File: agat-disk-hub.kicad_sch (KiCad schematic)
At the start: 14 parts, among them J1 IDC‐20, J2 IDC‐20, J3 IDC‐34, J4 IDC‐10, J5 KK‐4

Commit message: refactor: rename project to agat-disk-hub; add URL to back side; add J5 label
Old project name was agat_disk_adapter.
The permanent URL of the project is now http://museum.computer/re/agat-disk-hub
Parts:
- J1, J2: footprint agat_disk_adapter:IDC-20_header_vertical_rotation180 -> agat-disk-hub:IDC-20_header_vertical_rotation180
- J3: footprint agat_disk_adapter:IDC-34_header_vertical_rotation0 -> agat-disk-hub:IDC-34_header_vertical_rotation0
- J4: footprint agat_disk_adapter:IDC-10_header_vertical_rotation270 -> agat-disk-hub:IDC-10_header_vertical_rotation270
- J5: footprint agat_disk_adapter:Molex_KK-4_vertical_rotation0 -> agat-disk-hub:Molex_KK-4_vertical_rotation0
- JP1, JP2: footprint agat_disk_adapter:jumper_pins_solder_drop_vertical -> agat-disk-hub:jumper_pins_solder_drop_vertical
- R2: footprint agat_disk_adapter:jumper_1206_solder_drop -> agat-disk-hub:jumper_1206_solder_drop
- XP1: footprint agat_disk_adapter:Eltra-26M -> agat-disk-hub:Eltra-26M; symbol agat_disk_adapter:Eltra-26M -> agat-disk-hub:Eltra-26M
- XS1: footprint agat_disk_adapter:Eltra-26F -> agat-disk-hub:Eltra-26F; symbol agat_disk_adapter:Eltra-26F -> agat-disk-hub:Eltra-26F
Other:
- company: КИБЕР-МУЗЕЙ, МУРОМ - Михаил Шевченко - mike.shevchenko@gmail.com -> КИБЕР‐МУЗЕЙ, МУРОМ, Михаил Шевченко, http://museum.computer/re/agat-disk-hub
- title: AGAT DISK ADAPTER -> AGAT-DISK-HUB
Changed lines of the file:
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@@
 	(paper "A5" portrait)
 	(title_block
-		(title "AGAT DISK ADAPTER")
+		(title "AGAT-DISK-HUB")
 		(date "2026-09")
 		(rev "V1")
-		(company "КИБЕР-МУЗЕЙ, МУРОМ - Михаил Шевченко - mike.shevchenko@gmail.com")
-		(comment 1 "- Подключение КНГМД - штатным кабелем, либо шлейфом с СНП34-30 на IDC-20,")
-		(comment 2 "- Сигнал \"Выбор Блока\" для 2-го дисковода (ВБ2) можно завести через -12|DE2.")
-		(comment 3 "- Назначение дисководов 1-м и 2-м можно выполнить джамперами либо тумблерами.")
+		(company "КИБЕР‐МУЗЕЙ, МУРОМ, Михаил Шевченко, http://museum.computer/re/agat-disk-hub")
+		(comment 1 "- Подключение КНГМД - штатным кабелем, либо шлейфом с СНП34‐30 на IDC‐20.")
+		(comment 2 "- Сигнал \"Выбор Блока\" для 2‐го дисковода (ВБ2) можно завести через -12|DE2.")
+		(comment 3 "- Назначение дисководов 1‐м/2‐м можно выполнить джамперами либо тумблерами.")
 		(comment 4 "Плата для подключения дисководов 140К и их эмуляторов к КНГМД Агат-7 и Apple 2.")
 	)
@@
 	)
 	(symbol
-		(lib_id "agat_disk_adapter:Eltra-26M")
+		(lib_id "agat-disk-hub:Eltra-26M")
 		(at 91.44 74.93 0)
 		(unit 1)
@@
 			)
 		)
-		(property "Footprint" "agat_disk_adapter:Eltra-26M"
+		(property "Footprint" "agat-disk-hub:Eltra-26M"
 			(at 91.44 74.93 0)
 			(hide yes)
@@
 		)
 		(instances
-			(project "agat_disk_adapter"
+			(project "agat-disk-hub"
 				(path "/e6908ff4-84b7-4cdb-b4c1-fd2e829eca09"
 					(reference "XP1")
@@
 		)
 		(instances
-			(project "agat_disk_adapter"
+			(project "agat-disk-hub"
 				(path "/e6908ff4-84b7-4cdb-b4c1-fd2e829eca09"
 					(reference "#PWR06")
@@
 		)
 		(instances
-			(project "agat_disk_adapter"
+			(project "agat-disk-hub"
 				(path "/e6908ff4-84b7-4cdb-b4c1-fd2e829eca09"
 					(reference "XS404")
@@
 		)
 		(instances
-			(project "agat_disk_adapter"
+			(project "agat-disk-hub"
 				(path "/e6908ff4-84b7-4cdb-b4c1-fd2e829eca09"
 					(reference "#PWR09")
@@
 		)
 		(instances
-			(project "agat_disk_adapter"
+			(project "agat-disk-hub"
 				(path "/e6908ff4-84b7-4cdb-b4c1-fd2e829eca09"
 					(reference "#PWR011")
@@
 	)
 	(symbol
-		(lib_id "agat_disk_adapter:Eltra-26F")
+		(lib_id "agat-disk-hub:Eltra-26F")
 		(at 91.44 39.37 0)
 		(unit 1)
@@
 			)
 		)
-		(property "Footprint" "agat_disk_adapter:Eltra-26F"
+		(property "Footprint" "agat-disk-hub:Eltra-26F"
 			(at 91.44 39.37 0)
 			(hide yes)
@@
 		)
 		(instances
-			(project "agat_disk_adapter"
+			(project "agat-disk-hub"
 				(path "/e6908ff4-84b7-4cdb-b4c1-fd2e829eca09"
 					(reference "XS1")
@@
 			)
 		)
-		(property "Footprint" "agat_disk_adapter:IDC-34_header_vertical_rotation0"
+		(property "Footprint" "agat-disk-hub:IDC-34_header_vertical_rotation0"
 			(at 106.68 152.4 0)
 			(hide yes)
@@
 		)
 		(instances
-			(project "agat_disk_adapter"
+			(project "agat-disk-hub"
 				(path "/e6908ff4-84b7-4cdb-b4c1-fd2e829eca09"
 					(reference "J3")
@@
 		)
 		(instances
-			(project "agat_disk_adapter"
+			(project "agat-disk-hub"
 				(path "/e6908ff4-84b7-4cdb-b4c1-fd2e829eca09"
 					(reference "#PWR02")
@@
 			)
 		)
-		(property "Footprint" "agat_disk_adapter:Molex_KK-4_vertical_rotation0"
+		(property "Footprint" "agat-disk-hub:Molex_KK-4_vertical_rotation0"
 			(at 40.64 128.27 0)
 			(hide yes)
@@
 		)
 		(instances
-			(project "agat_disk_adapter"
+			(project "agat-disk-hub"
 				(path "/e6908ff4-84b7-4cdb-b4c1-fd2e829eca09"
 					(reference "J5")
@@
 			)
 		)
-		(property "Footprint" "agat_disk_adapter:IDC-20_header_vertical_rotation180"
+		(property "Footprint" "agat-disk-hub:IDC-20_header_vertical_rotation180"
 			(at 111.76 121.92 0)
 			(hide yes)
@@
 		)
 		(instances
-			(project "agat_disk_adapter"
+			(project "agat-disk-hub"
 				(path "/e6908ff4-84b7-4cdb-b4c1-fd2e829eca09"
 					(reference "J2")
@@
 		)
 		(instances
-			(project "agat_disk_adapter"
+			(project "agat-disk-hub"
 				(path "/e6908ff4-84b7-4cdb-b4c1-fd2e829eca09"
 					(reference "#PWR04")
@@
 		)
 		(instances
-			(project "agat_disk_adapter"
+			(project "agat-disk-hub"
 				(path "/e6908ff4-84b7-4cdb-b4c1-fd2e829eca09"
 					(reference "#PWR08")
@@
 		)
 		(instances
-			(project "agat_disk_adapter"
+			(project "agat-disk-hub"
 				(path "/e6908ff4-84b7-4cdb-b4c1-fd2e829eca09"
 					(reference "R1")
@@
 			)
 		)
-		(property "Footprint" "agat_disk_adapter:jumper_pins_solder_drop_vertical"
+		(property "Footprint" "agat-disk-hub:jumper_pins_solder_drop_vertical"
 			(at 129.54 132.08 0)
 			(hide yes)
@@
 		)
 		(instances
-			(project "agat_disk_adapter"
+			(project "agat-disk-hub"
 				(path "/e6908ff4-84b7-4cdb-b4c1-fd2e829eca09"
 					(reference "JP2")
@@
 			)
 		)
-		(property "Footprint" "agat_disk_adapter:jumper_1206_solder_drop"
+		(property "Footprint" "agat-disk-hub:jumper_1206_solder_drop"
 			(at 41.91 113.792 90)
 			(hide yes)
@@
 		)
 		(instances
-			(project "agat_disk_adapter"
+			(project "agat-disk-hub"
 				(path "/e6908ff4-84b7-4cdb-b4c1-fd2e829eca09"
 					(reference "R2")
@@
 			)
 		)
-		(property "Footprint" "agat_disk_adapter:IDC-10_header_vertical_rotation270"
+		(property "Footprint" "agat-disk-hub:IDC-10_header_vertical_rotation270"
 			(at 40.64 101.6 0)
 			(hide yes)
@@
 		)
 		(instances
-			(project "agat_disk_adapter"
+			(project "agat-disk-hub"
 				(path "/e6908ff4-84b7-4cdb-b4c1-fd2e829eca09"
 					(reference "J4")
@@
 		)
 		(instances
-			(project "agat_disk_adapter"
+			(project "agat-disk-hub"
 				(path "/e6908ff4-84b7-4cdb-b4c1-fd2e829eca09"
 					(reference "XT1")
@@
 		)
 		(instances
-			(project "agat_disk_adapter"
+			(project "agat-disk-hub"
 				(path "/e6908ff4-84b7-4cdb-b4c1-fd2e829eca09"
 					(reference "JP3")
@@
 		)
 		(instances
-			(project "agat_disk_adapter"
+			(project "agat-disk-hub"
 				(path "/e6908ff4-84b7-4cdb-b4c1-fd2e829eca09"
 					(reference "#PWR010")
@@
 		)
 		(instances
-			(project "agat_disk_adapter"
+			(project "agat-disk-hub"
 				(path "/e6908ff4-84b7-4cdb-b4c1-fd2e829eca09"
 					(reference "XS404")
@@
 		)
 		(instances
-			(project "agat_disk_adapter"
+			(project "agat-disk-hub"
 				(path "/e6908ff4-84b7-4cdb-b4c1-fd2e829eca09"
 					(reference "#PWR012")
@@
 		)
 		(instances
-			(project "agat_disk_adapter"
+			(project "agat-disk-hub"
 				(path "/e6908ff4-84b7-4cdb-b4c1-fd2e829eca09"
 					(reference "XS404")
@@
 		)
 		(instances
-			(project "agat_disk_adapter"
+			(project "agat-disk-hub"
 				(path "/e6908ff4-84b7-4cdb-b4c1-fd2e829eca09"
 					(reference "#PWR01")
@@
 		)
 		(instances
-			(project "agat_disk_adapter"
+			(project "agat-disk-hub"
 				(path "/e6908ff4-84b7-4cdb-b4c1-fd2e829eca09"
 					(reference "#PWR07")
@@
 		)
 		(instances
-			(project "agat_disk_adapter"
+			(project "agat-disk-hub"
 				(path "/e6908ff4-84b7-4cdb-b4c1-fd2e829eca09"
 					(reference "#PWR05")
@@
 			)
 		)
-		(property "Footprint" "agat_disk_adapter:IDC-20_header_vertical_rotation180"
+		(property "Footprint" "agat-disk-hub:IDC-20_header_vertical_rotation180"
 			(at 111.76 93.98 0)
 			(hide yes)
@@
 		)
 		(instances
-			(project "agat_disk_adapter"
+			(project "agat-disk-hub"
 				(path "/e6908ff4-84b7-4cdb-b4c1-fd2e829eca09"
 					(reference "J1")
@@
 		)
 		(instances
-			(project "agat_disk_adapter"
+			(project "agat-disk-hub"
 				(path "/e6908ff4-84b7-4cdb-b4c1-fd2e829eca09"
 					(reference "#PWR03")
@@
 			)
 		)
-		(property "Footprint" "agat_disk_adapter:jumper_pins_solder_drop_vertical"
+		(property "Footprint" "agat-disk-hub:jumper_pins_solder_drop_vertical"
 			(at 129.54 104.14 0)
 			(hide yes)
@@
 		)
 		(instances
-			(project "agat_disk_adapter"
+			(project "agat-disk-hub"
 				(path "/e6908ff4-84b7-4cdb-b4c1-fd2e829eca09"
 					(reference "JP1")

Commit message: remove -12|DE2 option with JP1, rename JP3 to JP1 and move to its old place; label JP2 as FW307
The option of supplying DE2 via +12 wire on IDC-20 or Eltra is considered dangerous for controllers
(if someone plugs a standard cable with -12 into our board with this jumper on), so it is removed
together with its JP1; the Net -12|DE renamed to just -12.

JP3 (jumper parking ground) is renamed to JP1 and moved to the place previously occupied by JP1.

Other minor adjustments:
- Adjust a few J3 traces.
- Adjust silk items, including:
  - The "jumper parking" label made bigger, as a regular Function front-side label.
  - The "(FW 307)" label at JP2 becomes its Function on the Schematics and now reads "FW307".
  - Remove back side brackets for XP1 and J1.
  - Center horitontal labels by their coordinate, not by the visually occupied space.
  - Make the text of knocked-out labels bolder.
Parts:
- removed JP1: PLS‐2, agat-disk-hub:jumper_pins_solder_drop_vertical, symbol Connector:Conn_01x02_Pin
- removed XT1: PLS‐1, Connector_PinHeader_2.00mm:PinHeader_1x01_P2.00mm_Vertical, symbol Connector:Conn_01x01_Pin
- JP1: renamed from JP3; Function ДЕРЖ. ДЖАМПЕРОВ -> ДЕРЖ.ДЖ.
- JP2: Function Ф1C→G.32 -> FW307
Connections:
- net -12|DE2 is gone; now on net -12: J1.9 (Pin_9), J2.9 (Pin_9), XP1.A9 (N/U), XS1.A9 (N/U)
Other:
- moved on the sheet: JP1

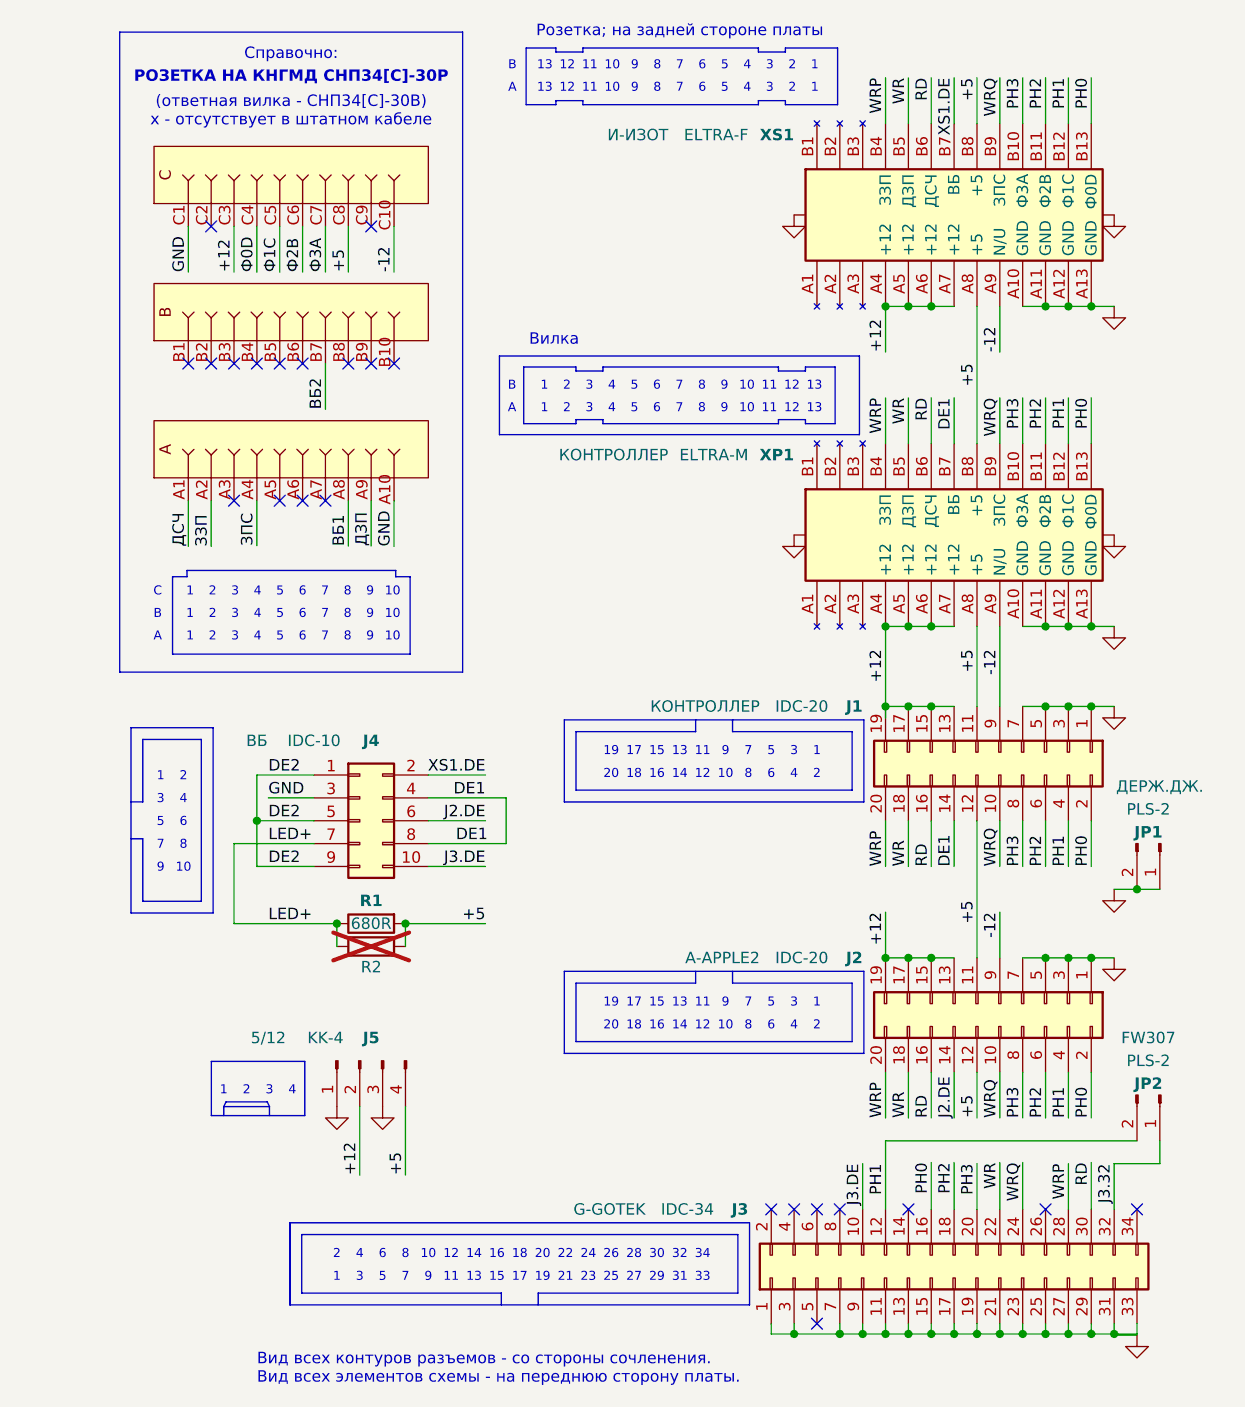
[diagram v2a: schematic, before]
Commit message: remap J3 phase pins, drop FW307 jumper, restore XT1; rework symbols, silkscreen and mask
Electrical:
- J3: PH0 moves from pin 16 to pin 4, PH1 from pin 12 to pin 16, and pin 12 is left
  unconnected; tracks rerouted to match. This is needed to enable identical wiring inside Goteks
  for use with PC/Spectrum or Apple2/Agat.
- JP2, the FW307 jumper, is removed: J3 pin 32 is tied to PH1 for good - the PH0/PH1 remapping
  allows it for all use cases.
- Fixed: XT1 connector was of type 2.0 mm, now is the proper 2.54 mm (since it's just one pin, it
  defines its size); adjusted the connector position.

Schematic and symbols (refactoring only):
- XT1 is back on the schematic on DE2, after being lost together with the old JP1.
- XS404, the SNP34 cable connector, uses new project symbol SNP34-30R, whose pin names match its
  wiring.
- Eltra-26F and Eltra-26M: origin moved to pin A7, made other symbol improvements.
- J3: pin 5 is removed from the symbol copy in the schematic and from the IDC-34 library
  footprint.
- Used PWR_FLAG on GND in place of one GND symbol; made ERC exclusions for the custom footprints,
  keyed J3, and one four-way junction.
- Added note to R2 as an SMD alternative to R1, or a bridge for LEDs taking +5.
- Title block: dated 2026-10-08, deleted obsolete comment on -12|DE2.

Silkscreen and mask:
- The three museum logo footprints are replaced by the museum's name as text on F.Mask, in
  the `Agat-7 7x8px` font.
- Back: the J1 and J2 signal label rows swap places, GND texts become drawn ground marks, +5 labels
  get leader lines, pin-count labels are rotated, and row letters moved.
- Front: XS1 gets A/B row letters, the KK power connector marked as VYKHOD (output), XT1 gets a
  `(B7)` note to show its pin on the controller side.
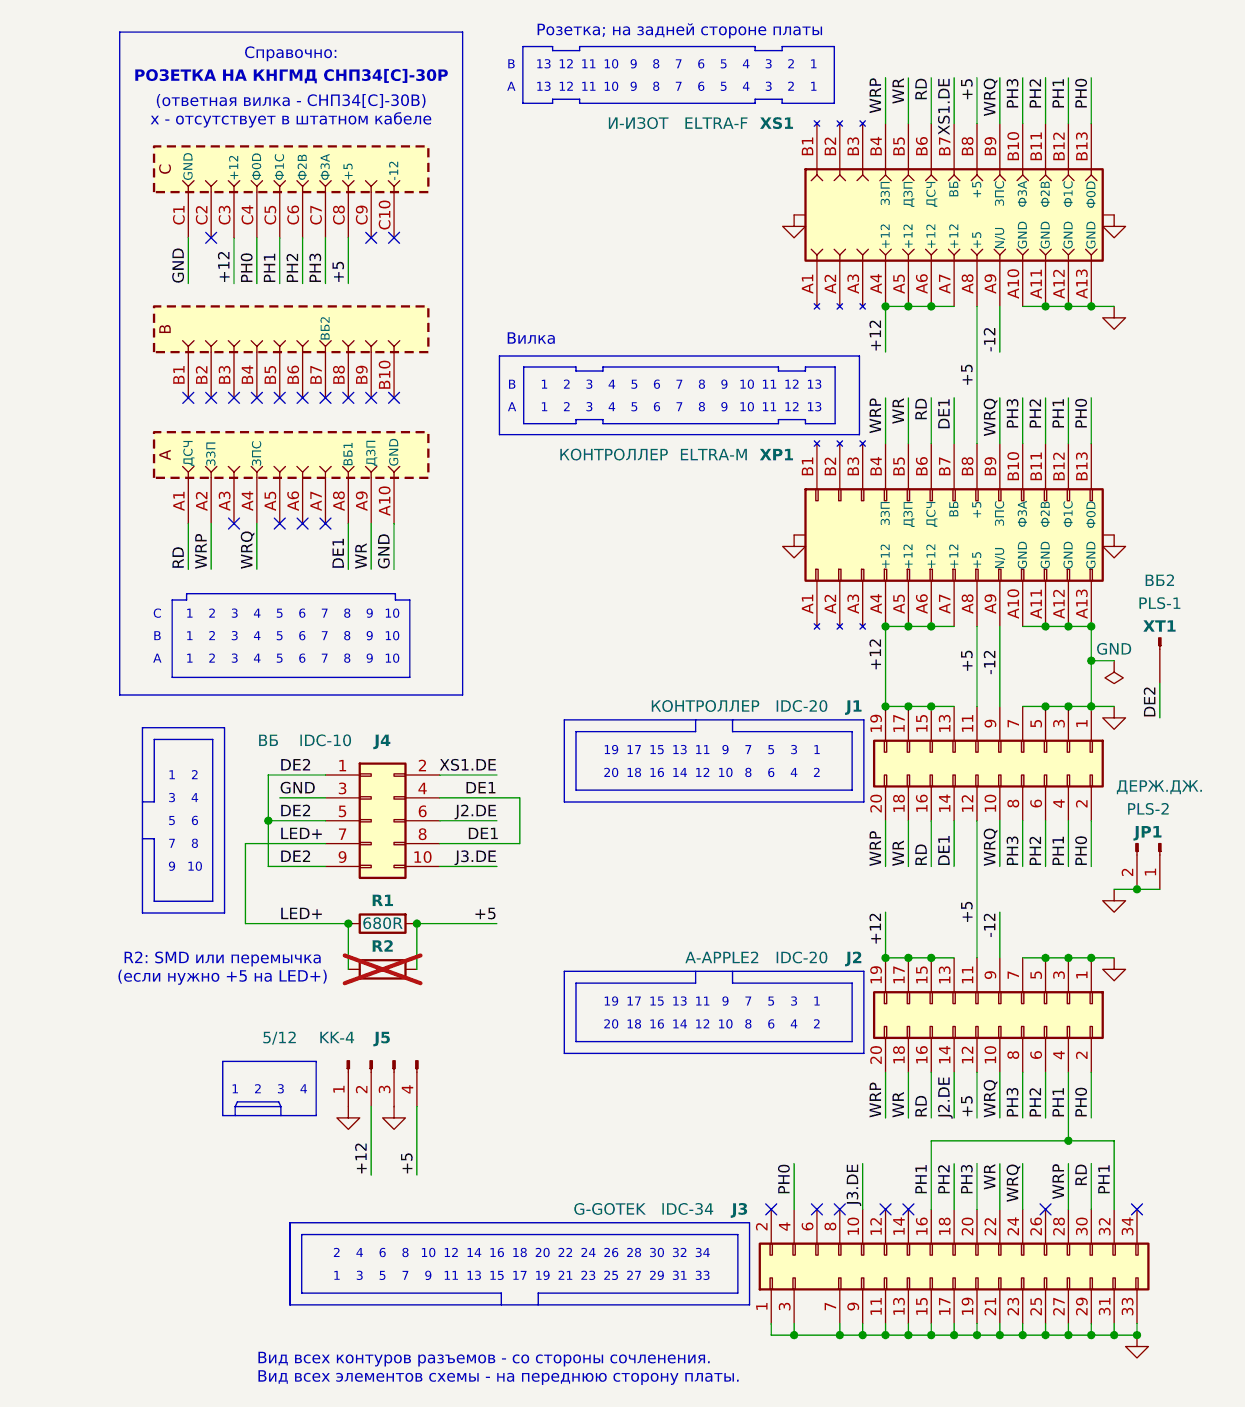
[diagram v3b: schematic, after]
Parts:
- removed JP2: PLS‐2, agat-disk-hub:jumper_pins_solder_drop_vertical, symbol Connector:Conn_01x02_Pin
- added XT1: PLS‐1, Connector_PinHeader_2.54mm:PinHeader_1x01_P2.54mm_Vertical, symbol Connector:Conn_01x01_Pin
- XS404: value СНП34С-30/44-12 -> СНП34-30Р; symbol agat-lib:СНП34С-30/44-12 -> agat-disk-hub:СНП34-30Р
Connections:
- net J3.32 is gone; now on net PH1: J3.32 (Pin_32)
- net ВБ1 is gone; now on net DE1: XS404.A8 (ВБ1)
- net ДЗП is gone; now on net WR: XS404.A9 (ДЗП)
- net ДСЧ is gone; now on net RD: XS404.A1 (ДСЧ)
- net ЗЗП is gone; now on net WRP: XS404.A2 (ЗЗП)
- net ЗПС is gone; now on net WRQ: XS404.A4 (ЗПС)
- net Ф0D is gone; now on net PH0: XS404.C4 (Ф0D)
- net Ф1C is gone; now on net PH1: XS404.C5 (Ф1C)
- net Ф2B is gone; now on net PH2: XS404.C6 (Ф2B)
- net Ф3A is gone; now on net PH3: XS404.C7 (Ф3A)
- net -12: no longer XS404.C10
- net DE2: now also XT1.1 (Pin_1)
- net PH0: now also J3.4 (Pin_4); no longer J3.16 (Pin_16)
- net PH1: now also J3.16 (Pin_16); no longer J3.12 (Pin_12)
- net ВБ2: no longer names the net of XS404.B7 (ВБ2)
- no-connect marks 23 -> 24
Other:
- note added: "(ответная вилка - СНП34[С]‐30В) х - отсутствует в штатном кабеле"
- note added: "R2: SMD или перемычка (если нужно +5 на LED+)"
- note added: "РОЗЕТКА НА КНГМД СНП34[С]‐30Р"
- note removed: "(ответная вилка - СНП34[С]-30В) х - отсутствует в штатном кабеле"
- note removed: "РОЗЕТКА НА КНГМД СНП34[С]-30Р"
- moved on the sheet: J4, J5, R1, R2
